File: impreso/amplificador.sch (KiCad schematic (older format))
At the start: 93 parts, among them Q1 MPSA92, Q10 MPSA42, Q11 MPSA42, Q1201 MPSA92, Q1202 MPSA92, Q14 MJE340, Q15 MJE350, Q1501 MPSA42, Q1502 MPSA42, Q16 MJE340, Q17 MJE350, Q18 2SC3281, Q19 2SC3281, Q2 MPSA92, Q20 2SA1302, Q21 2SA1302, Q3 MPSA42, Q4 MPSA42, Q501 MPSA92, Q502 MPSA92, Q701 MPSA92, Q702 MPSA92, Q801 MJE350, Q802 MJE340, T1 TORNILLO, T2 TORNILLO, T3 TORNILLO, T4 TORNILLO, T5 TORNILLO, T6 TORNILLO, T7 TORNILLO, T8 TORNILLO

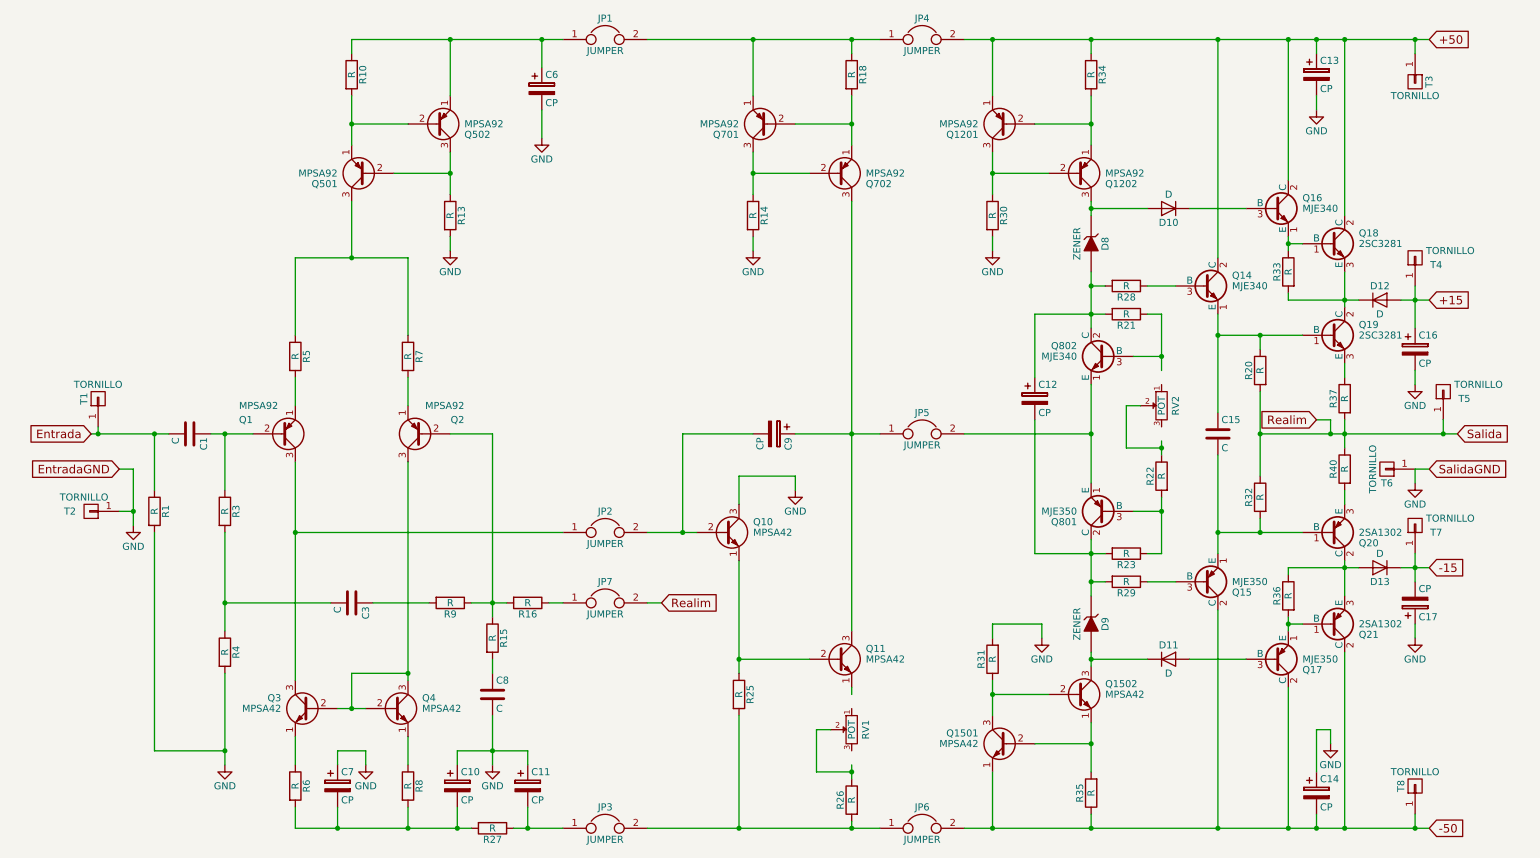
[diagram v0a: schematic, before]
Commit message: Terminado el esquemático armado a partir de ampli-exp.asc, empiezo el PCB.
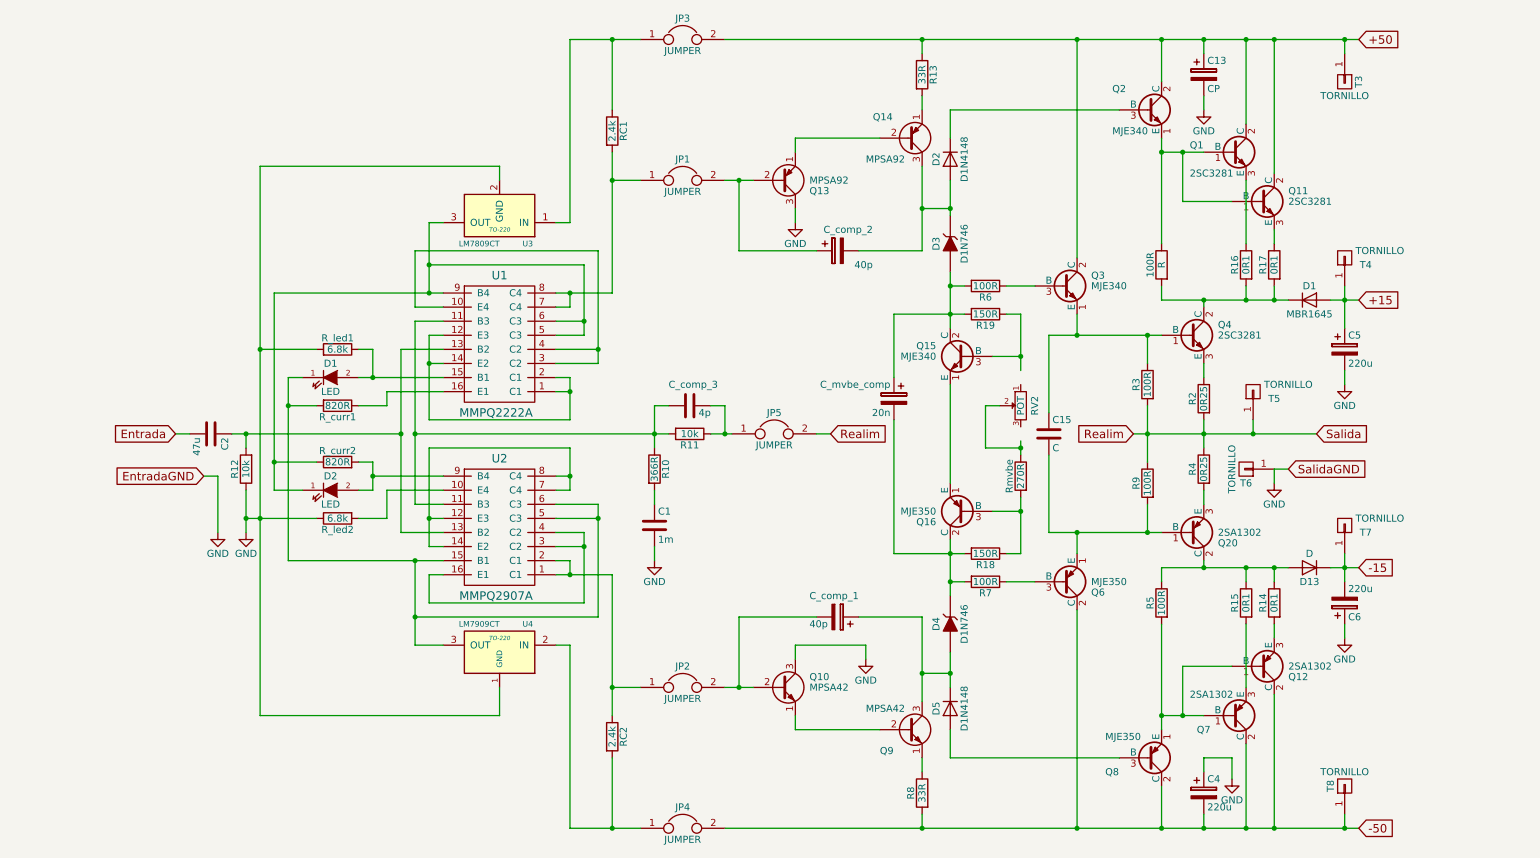
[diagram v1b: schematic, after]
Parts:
- removed C1, C3: C, Capacitors_Elko_ThroughHole:Elko_vert_11.5x8mm_RM3.5, symbol C
- removed C10, C11, C6, C7: CP, Capacitors_Elko_ThroughHole:Elko_vert_11.5x8mm_RM3.5, symbol CP
- removed JP4, JP5, JP6: JUMPER, Pin_Headers:Pin_Header_Straight_1x02, symbol JUMPER
- removed Q1, Q1201, Q1202, Q2, Q501, Q502, Q701: MPSA92, Housings_TO-92:TO-92_Inline_Narrow_Oval, symbol MPSA92
- removed Q1501, Q1502, Q3, Q4: MPSA42, Housings_TO-92:TO-92_Inline_Narrow_Oval, symbol MPSA42
- removed R1, R10, R13, R25, R3, R30, R31, R34, R35, R36, R4, R7, R8, R9: R, Resistors_ThroughHole:Resistor_Horizontal_RM10mm, symbol R
- removed R27: R, Resistors_ThroughHole:Resistor_Horizontal_RM20mm, symbol R
- removed RV1: POT, Potentiometers:Potentiometer_Bourns_3296W_3-8Zoll_Inline_ScrewUp, symbol POT
- removed T1, T2: TORNILLO, bibliotecas:TORNILLO, symbol TORNILLO
- added C2: 47u, Capacitors_Elko_ThroughHole:Elko_vert_11.5x8mm_RM3.5, symbol C
- added C_comp_2: 40p, Capacitors_Elko_ThroughHole:Elko_vert_11.5x8mm_RM3.5, symbol CP
- added C_comp_3: 4p, Capacitors_Elko_ThroughHole:Elko_vert_11.5x8mm_RM3.5, symbol C
- added D1, D2: LED, symbol LED
- added JP3: JUMPER, Pin_Headers:Pin_Header_Straight_1x02, symbol JUMPER
- added Q11: 2SC3281, bibliotecas:DT-25-B01W-03, symbol 2SC3281
- added Q12: 2SA1302, bibliotecas:DT-25-B01W-03, symbol 2SA1302
- added Q13: MPSA92, Housings_TO-92:TO-92_Inline_Narrow_Oval, symbol MPSA92
- added R12: 10k, Resistors_ThroughHole:Resistor_Horizontal_RM10mm, symbol R
- added R15, R16, R17: 0R1, Resistors_ThroughHole:Resistor_Horizontal_RM10mm, symbol R
- added RC1: 2.4k, Resistors_ThroughHole:Resistor_Horizontal_RM10mm, symbol R
- added R_curr1, R_curr2: 820R, Resistors_ThroughHole:Resistor_Horizontal_RM10mm, symbol R
- added R_led1, R_led2: 6.8k, Resistors_ThroughHole:Resistor_Horizontal_RM10mm, symbol R
- added U1: MMPQ2222A, pcb:SOIC-16, symbol MMPQ2222A
- added U2: MMPQ2907A, pcb:SOIC-16, symbol MMPQ2907A
- added U3: LM7809CT, TO-220, symbol LM7809CT
- added U4: LM7909CT, TO-220, symbol LM7909CT
- C1: renamed from C8; value C -> 1m
- C4: renamed from C14; value CP -> 220u
- C5: renamed from C16; value CP -> 220u
- C6: renamed from C17; value CP -> 220u
- C_comp_1: renamed from C9; value CP -> 40p
- C_mvbe_comp: renamed from C12; value CP -> 20n
- D1: renamed from D12; value D -> MBR1645
- D2: renamed from D10; value D -> D1N4148
- D3: renamed from D8; value ZENER -> D1N746
- D4: renamed from D9; value ZENER -> D1N746
- D5: renamed from D11; value D -> D1N4148
- R10: renamed from R15; value R -> 366R
- R11: renamed from R16; value R -> 10k
- R13: renamed from R18; value R -> 33R
- R14: value R -> 0R1
- R18: renamed from R23; value R -> 150R
- R19: renamed from R21; value R -> 150R
- R2: renamed from R37; value R -> 0R25
- R3: renamed from R20; value R -> 100R
- R4: renamed from R40; value R -> 0R25
- R5: value R -> 100R
- R6: renamed from R28; value R -> 100R
- R7: renamed from R29; value R -> 100R
- R8: renamed from R26; value R -> 33R
- R9: renamed from R32; value R -> 100R
- RC2: renamed from R6; value R -> 2.4k
- Rmvbe: renamed from R22; value R -> 270R
- renumbered R33 to 100R, JP3 to JP4, JP7 to JP5, Q18 to Q1, Q702 to Q14, Q802 to Q15, Q801 to Q16, Q16 to Q2, Q14 to Q3, Q19 to Q4, Q15 to Q6, Q21 to Q7, Q17 to Q8, Q11 to Q9
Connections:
- net +50: now also R13.1, JP3.2, Q11.2 (C)
- net -50: now also JP4.2, R8.2, Q12.2 (C)
- net Entrada: now also C2.2
- net GND: now also Q13.3 (C), R12.1, R_led1.2, R_led2.1, U3.2 (GND), U4.1 (GND); no longer R14.2
- net at JP1.1: now also RC1.2, U1.7 (C4), U1.8 (C4)
- net at R5.1: now also D13.2 (A), Q20.2 (C), R14.1, R15.1
- net at R5.2: now also Q7.1 (B), Q8.1 (E), Q12.1 (B)
- net at R10.1, R11.2: now also C_comp_3.1, U1.11 (B3), U2.11 (B3)
- net at JP2.1: now also RC2.1, U2.1 (C1), U2.2 (C1)
- net at RC2.2: now also JP4.1, U4.2 (IN)
- net at JP1.2: now also C_comp_2.1, Q13.2 (B); no longer R13.1
- net at Q14.2 (B): now also Q13.1 (E); no longer R14.1
- net at C_comp_1.1, Q9.3 (C): now also D4.2 (A), D5.1 (K); no longer Q14.3 (C)
- net at Q9.1 (E): now also R8.1
- net at D2.2 (A), D3.1 (K): now also Q14.3 (C), C_comp_2.2
- net at 100R.1, Q1.1 (B), Q2.1 (E): now also Q11.1 (B)
- net at 100R.2, D1.1 (K), Q4.2 (C): now also R16.2, R17.2; no longer Q1.3 (E)
- net at JP5.1, R11.1: now also C_comp_3.2
- new net: Q1.3 (E), R16.1
- new net: Q7.3 (E), R15.2
- new net: Q12.3 (E), R14.2
- new net: Q11.3 (E), R17.1
- new net: JP3.1, RC1.1, U3.1 (IN)
- new net: U1.1 (C1), U1.12 (E3), U1.14 (E2), U1.2 (C1)
- new net: U1.10 (E4), U1.3 (C2), U1.4 (C2)
- new net: C2.1, R12.2, U1.13 (B2), U2.13 (B2)
- new net: D1.2 (A), R_led1.1, U1.15 (B1)
- new net: R_curr1.1, U1.16 (E1)
- new net: D2.1 (K), R_curr2.1, U1.5 (C3), U1.6 (C3), U1.9 (B4), U3.3 (OUT)
- new net: D1.1 (K), R_curr1.2, U2.15 (B1), U2.5 (C3), U2.6 (C3), U4.3 (OUT)
- new net: R_led2.2, U2.10 (E4)
- new net: U2.12 (E3), U2.14 (E2), U2.7 (C4), U2.8 (C4)
- new net: U2.16 (E1), U2.3 (C2), U2.4 (C2)
- new net: D2.2 (A), R_curr2.2, U2.9 (B4)
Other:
- moved on the sheet: 100R, C1, C13, C15, C4, C5, C6, C_comp_1, C_mvbe_comp, D1, D13, D2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

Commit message: Esta casi listo el PCB, necesito ayuda, ensanchen las pistas de potencia, pongan un plano de masa atrás, para vincular todos los componentes que falta mandar a masa, y hacen falta un par de vías.
Con más tiempo, lo dejaría mejor, pero es un quilombo. Tendría que comparar como hice la vez pasada, que me quedó de re chupete.
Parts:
- C1, C2, C_comp_3: footprint Capacitors_Elko_ThroughHole:Elko_vert_11.5x8mm_RM3.5 -> Capacitors_ThroughHole:C_Rect_L7_W3.5_P5
- C3: renamed from C15; value C -> 10n; footprint Capacitors_Elko_ThroughHole:Elko_vert_11.5x8mm_RM3.5 -> Capacitors_ThroughHole:C_Rect_L7_W3.5_P5
- C4, C5, C6, C_comp_1, C_comp_2: footprint Capacitors_Elko_ThroughHole:Elko_vert_11.5x8mm_RM3.5 -> Discret:CP5
- C7: renamed from C13; value CP -> 220u; footprint Capacitors_Elko_ThroughHole:Elko_vert_11.5x8mm_RM3.5 -> Discret:CP5
- C_mvbe_comp1: renamed from C_mvbe_comp; footprint Capacitors_ThroughHole:C_Rect_L18_W5_P15 -> Discret:CP5
- D_1: renamed from D1; footprint (none) -> LEDs:LED-5MM
- D_2: renamed from D2; footprint (none) -> LEDs:LED-5MM
- Q10, Q13, Q14, Q9: footprint Housings_TO-92:TO-92_Inline_Narrow_Oval -> TO_SOT_Packages_THT:TO-92_Horizontal1_Inline_Narrow_Oval
- Q2, Q3, Q6, Q8: footprint Housings_SOT:SOT126_SOT32_Housing_Vertical -> TO_SOT_Packages_THT:SOT126_SOT32_Housing_Vertical
- R1: renamed from 100R; value R -> 100R
- R14, R15, R16, R17: footprint Resistors_ThroughHole:Resistor_Horizontal_RM10mm -> Resistors_ThroughHole:Resistor_Ceramic_Horizontal_L36mm-W11mm-H10mm-p45mm
- U3, U4: footprint TO-220 -> Power_Integrations:TO-220
- renumbered Rmvbe to Rmvbe1
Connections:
- net +15: now also U3.1 (IN)
- net -15: now also U4.2 (IN)
- net at JP4.1, RC2.2: no longer U4.2 (IN)
- net at JP3.1, RC1.1: no longer U3.1 (IN)
- net at R_curr2.1, U1.5 (C3), U1.6 (C3)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: now also D_2.2 (A); no longer D_2.1 (K)
- net at U2.10 (E4): now also R_curr2.2; no longer R_led2.2
- new net: D_2.1 (K), R_led2.2, U2.9 (B4)
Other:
- moved on the sheet: R_curr2, R_led2

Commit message: Agregué la Red de Zobel.
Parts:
- added Czobel1: 100n, Capacitors_ThroughHole:C_Rect_L7_W3.5_P5, symbol C
- added Rzobel1: 10R, Resistors_ThroughHole:Resistor_Horizontal_RM10mm, symbol R
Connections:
- net GND: now also Czobel1.1
- net Realim: now also Rzobel1.1
- new net: Czobel1.2, Rzobel1.2
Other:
- moved on the sheet: T6
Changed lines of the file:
@@
 U 1 1 5596AC4F
 P 8800 4300
-F 0 "Q20" H 9000 4375 50  0000 L CNN
-F 1 "2SA1302" H 9000 4300 50  0000 L CNN
+F 0 "Q20" H 8550 4150 50  0000 L CNN
+F 1 "2SA1302" H 8450 4450 50  0000 L CNN
 F 2 "bibliotecas:DT-25-B01W-03" H 9000 4225 50  0001 L CIN
 F 3 "" H 8800 4300 50  0000 L CNN
@@
 Text GLabel 10000 800  2    60   Input ~ 0
 +50
-Text GLabel 9700 3600 2    60   Input ~ 0
+Text GLabel 9950 3600 2    60   Input ~ 0
 Salida
 $Comp
@@
 	1    0    0    -1
 $EndComp
-Text GLabel 9500 3850 2    60   Input ~ 0
+Text GLabel 9750 3800 2    60   Input ~ 0
 SalidaGND
 $Comp
 L GND #PWR06
 U 1 1 559EDF98
-P 9400 3950
-F 0 "#PWR06" H 9400 3700 50  0001 C CNN
-F 1 "GND" H 9400 3800 50  0000 C CNN
-F 2 "" H 9400 3950 60  0000 C CNN
-F 3 "" H 9400 3950 60  0000 C CNN
-	1    9400 3950
+P 9650 4200
+F 0 "#PWR06" H 9650 3950 50  0001 C CNN
+F 1 "GND" H 9650 4050 50  0000 C CNN
+F 2 "" H 9650 4200 60  0000 C CNN
+F 3 "" H 9650 4200 60  0000 C CNN
+	1    9650 4200
 	1    0    0    -1
 $EndComp
@@
 L TORNILLO T6
 U 1 1 559797E2
-P 9200 3850
-F 0 "T6" H 9200 3950 50  0000 C CNN
-F 1 "TORNILLO" V 9300 3850 50  0000 C CNN
-F 2 "bibliotecas:TORNILLO" H 9200 3850 60  0001 C CNN
-F 3 "" H 9200 3850 60  0000 C CNN
-	1    9200 3850
+P 9450 3800
+F 0 "T6" H 9450 3900 50  0000 C CNN
+F 1 "TORNILLO" V 9550 3800 50  0000 C CNN
+F 2 "bibliotecas:TORNILLO" H 9450 3800 60  0001 C CNN
+F 3 "" H 9450 3800 60  0000 C CNN
+	1    9450 3800
 	-1   0    0    1
 $EndComp
@@
 	5400 3600 5550 3600
 Wire Wire Line
-	9400 3950 9400 3850
-Wire Wire Line
-	9400 3850 9500 3850
+	9650 3800 9650 4200
+Wire Wire Line
+	9650 3800 9750 3800
 Wire Wire Line
 	1800 3900 1900 3900
@@
 	4700 1300 4700 800
 Wire Wire Line
-	8400 3600 9700 3600
+	8400 3600 9950 3600
 Wire Wire Line
 	7800 3450 7800 2900
@@
 Connection ~ 2100 4200
 Connection ~ 2200 3800
+$Comp
+L R Rzobel1
+U 1 1 5670E41C
+P 9100 3800
+F 0 "Rzobel1" V 9180 3800 50  0000 C CNN
+F 1 "10R" V 9100 3800 50  0000 C CNN
+F 2 "Resistors_ThroughHole:Resistor_Horizontal_RM10mm" V 9030 3800 30  0001 C CNN
+F 3 "" H 9100 3800 30  0000 C CNN
+	1    9100 3800
+	1    0    0    -1
+$EndComp
+$Comp
+L C Czobel1
+U 1 1 5670E6F6
+P 9350 4100
+F 0 "Czobel1" V 9500 3900 50  0000 L CNN
+F 1 "100n" V 9400 3850 50  0000 L CNN
+F 2 "Capacitors_ThroughHole:C_Rect_L7_W3.5_P5" H 9388 3950 30  0001 C CNN
+F 3 "" H 9350 4100 60  0000 C CNN
+	1    9350 4100
+	0    1    1    0
+$EndComp
+Wire Wire Line
+	9100 3650 9100 3600
+Connection ~ 9100 3600
+Wire Wire Line
+	9100 3950 9100 4100
+Wire Wire Line
+	9100 4100 9200 4100
+Wire Wire Line
+	9650 4100 9500 4100
+Connection ~ 9650 4100
 $EndSCHEMATC

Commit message: Agregué resistencias de emisor, y resistencia a la salida. No pude agregar inductor, no lo encuentro en las bibliotecas.
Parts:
- added R20, R21: 1K, Resistors_ThroughHole:Resistor_Horizontal_RM10mm, symbol R
- added Rzobel?: 10R, Resistors_ThroughHole:Resistor_Horizontal_RM10mm, symbol R
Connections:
- net +50: now also R20.1
- net -50: now also R21.2
- net Realim: now also Rzobel?.2
- net at Q13.1 (E), Q14.2 (B): now also R20.2
- net at Q10.1 (E), Q9.2 (B): now also R21.1
- new net Salida: Rzobel?.1
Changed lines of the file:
@@
 	4700 1300 4700 800
-Wire Wire Line
-	8400 3600 9950 3600
 Wire Wire Line
 	7800 3450 7800 2900
@@
 	5000 3400 5000 3700
 Wire Wire Line
-	6000 1600 6000 1500
+	6000 1200 6000 1600
 Wire Wire Line
-	6000 5700 6000 5600
+	6000 5600 6000 6000
 Wire Wire Line
 	4700 800  4900 800
@@
 	9650 4100 9500 4100
 Connection ~ 9650 4100
+$Comp
+L R R21
+U 1 1 5672522D
+P 6000 6150
+F 0 "R21" V 6080 6150 50  0000 C CNN
+F 1 "1K" V 6000 6150 50  0000 C CNN
+F 2 "Resistors_ThroughHole:Resistor_Horizontal_RM10mm" V 5930 6150 30  0001 C CNN
+F 3 "" H 6000 6150 30  0000 C CNN
+	1    6000 6150
+	-1   0    0    -1
+$EndComp
+Connection ~ 6000 5700
+Wire Wire Line
+	6000 6300 6000 6400
+Connection ~ 6000 6400
+$Comp
+L R R20
+U 1 1 56726196
+P 6000 1050
+F 0 "R20" V 6080 1050 50  0000 C CNN
+F 1 "1K" V 6000 1050 50  0000 C CNN
+F 2 "Resistors_ThroughHole:Resistor_Horizontal_RM10mm" V 5930 1050 30  0001 C CNN
+F 3 "" H 6000 1050 30  0000 C CNN
+	1    6000 1050
+	1    0    0    -1
+$EndComp
+Wire Wire Line
+	6000 900  6000 800
+Connection ~ 6000 800
+Connection ~ 6000 1500
+$Comp
+L R Rzobel?
+U 1 1 56726E0F
+P 9600 3600
+F 0 "Rzobel?" V 9680 3600 50  0000 C CNN
+F 1 "10R" V 9600 3600 50  0000 C CNN
+F 2 "Resistors_ThroughHole:Resistor_Horizontal_RM10mm" V 9530 3600 30  0001 C CNN
+F 3 "" H 9600 3600 30  0000 C CNN
+	1    9600 3600
+	0    1    1    0
+$EndComp
+Wire Wire Line
+	8400 3600 9450 3600
+Wire Wire Line
+	9350 3600 9350 3450
+Wire Wire Line
+	9350 3450 9500 3450
+Connection ~ 9350 3600
+Wire Wire Line
+	9750 3600 9950 3600
+Wire Wire Line
+	9700 3450 9850 3450
+Wire Wire Line
+	9850 3450 9850 3600
+Connection ~ 9850 3600
 $EndSCHEMATC

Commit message: inductor
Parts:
- added L?: L_Small, symbol L_Small
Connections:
- net Realim: now also L?.1
- net Salida: now also L?.2
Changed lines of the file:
@@
 EESchema Schematic File Version 2
+LIBS:power
+LIBS:device
+LIBS:transistors
+LIBS:conn
+LIBS:linear
+LIBS:regul
+LIBS:74xx
+LIBS:cmos4000
+LIBS:adc-dac
+LIBS:memory
+LIBS:xilinx
+LIBS:microcontrollers
+LIBS:dsp
+LIBS:microchip
+LIBS:analog_switches
+LIBS:motorola
+LIBS:texas
+LIBS:intel
+LIBS:audio
+LIBS:interface
+LIBS:digital-audio
+LIBS:philips
+LIBS:display
+LIBS:cypress
+LIBS:siliconi
+LIBS:opto
+LIBS:atmel
+LIBS:contrib
+LIBS:valves
 LIBS:lib_ampli
 LIBS:amplificador-cache
@@
 	9850 3450 9850 3600
 Connection ~ 9850 3600
+$Comp
+L L_Small L?
+U 1 1 5672A668
+P 9600 3450
+F 0 "L?" H 9630 3490 50  0000 L CNN
+F 1 "L_Small" H 9630 3410 50  0000 L CNN
+F 2 "" H 9600 3450 50  0000 C CNN
+F 3 "" H 9600 3450 50  0000 C CNN
+	1    9600 3450
+	0    -1   -1   0
+$EndComp
+Entry Wire Line
+	6140 1790 6240 1890
 $EndSCHEMATC
